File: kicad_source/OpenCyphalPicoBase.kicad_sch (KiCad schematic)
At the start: 49 parts, among them CN1 RASPBERRYPI_PICO, CN11 DNI, CN12 S3B-PH-SM4-TB, CN2 SM04B-SRSS-TB, CN3 SM04B-SRSS-TB, CN6 691322310002, CN7 DNI, CN8 DNI, SW1 PTS636 SM43 SMTR LFS, U3 24LC64-I/SN

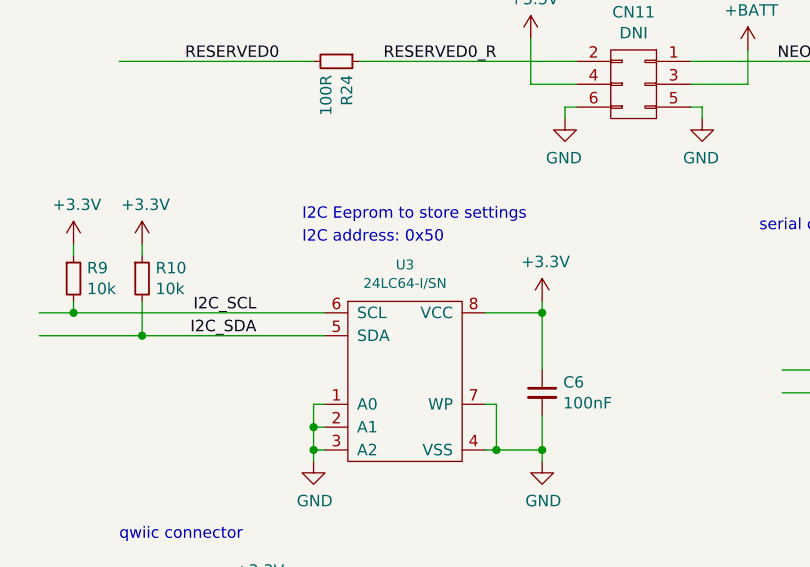
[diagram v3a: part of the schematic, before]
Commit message: switched to JLCPCB basic parts where possible
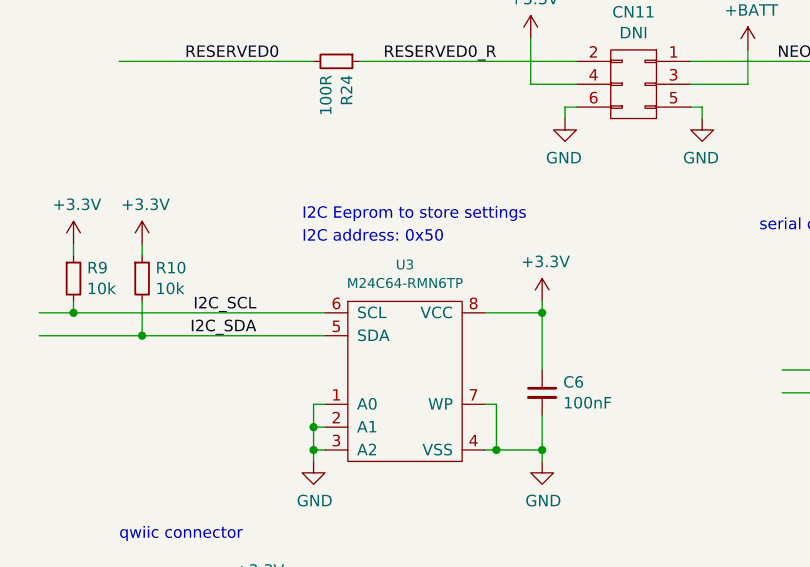
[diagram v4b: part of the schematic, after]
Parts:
- C1, C10, C2, C5, C6, C9: LCSC C314282 -> C14663
- R10, R14, R17, R18, R19, R4, R5, R6, R7, R8, R9: LCSC C3152123 -> C25804
- R11, R12, R20, R21, R22, R23, R24, R25: LCSC C105588 -> C22775
- R15, R16: LCSC C108078 -> C22978
- U3: value 24LC64-I/SN -> M24C64-RMN6TP; LCSC C3007892 -> C79988
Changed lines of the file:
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@@
     )
     (property "Datasheet" "" (id 3) (at 22.86 128.27 0))
-    (property "LCSC" "C3152123" (id 4) (at 22.86 128.27 0)
+    (property "LCSC" "C25804" (id 4) (at 22.86 128.27 0)
       (effects (font (size 1.27 1.27)) hide)
     )
@@
     )
     (property "Datasheet" "" (id 3) (at 30.48 128.27 0))
-    (property "LCSC" "C3152123" (id 4) (at 30.48 128.27 0)
+    (property "LCSC" "C25804" (id 4) (at 30.48 128.27 0)
       (effects (font (size 1.27 1.27)) hide)
     )
@@
     )
     (property "Datasheet" "" (id 3) (at 124.46 166.37 0))
-    (property "LCSC" "C105588" (id 4) (at 124.46 166.37 0)
+    (property "LCSC" "C22775" (id 4) (at 124.46 166.37 0)
       (effects (font (size 1.27 1.27)) hide)
     )
@@
     )
     (property "Datasheet" "" (id 3) (at 85.09 166.37 0))
-    (property "LCSC" "C105588" (id 4) (at 85.09 166.37 0)
+    (property "LCSC" "C22775" (id 4) (at 85.09 166.37 0)
       (effects (font (size 1.27 1.27)) hide)
     )
@@
       (effects (font (size 1.0922 1.0922)))
     )
-    (property "Value" "24LC64-I/SN" (id 1) (at 59.69 128.8034 0)
+    (property "Value" "M24C64-RMN6TP" (id 1) (at 59.69 128.8034 0)
       (effects (font (size 1.0922 1.0922)))
     )
@@
       (effects (font (size 1.0922 1.0922)) hide)
     )
-    (property "LCSC" "C3007892" (id 4) (at 59.69 139.7 0)
+    (property "LCSC" "C79988" (id 4) (at 59.69 139.7 0)
       (effects (font (size 1.27 1.27)) hide)
     )
@@
     )
     (property "Datasheet" "" (id 3) (at 74.93 140.97 0))
-    (property "LCSC" "C314282" (id 4) (at 74.93 140.97 0)
+    (property "LCSC" "C14663" (id 4) (at 74.93 140.97 0)
       (effects (font (size 1.27 1.27)) hide)
     )
@@
     )
     (property "Datasheet" "" (id 3) (at 259.08 63.5 0))
-    (property "LCSC" "C108078" (id 4) (at 259.08 63.5 0)
+    (property "LCSC" "C22978" (id 4) (at 259.08 63.5 0)
       (effects (font (size 1.27 1.27)) hide)
     )
@@
     )
     (property "Datasheet" "" (id 3) (at 270.51 63.5 0))
-    (property "LCSC" "C108078" (id 4) (at 270.51 63.5 0)
+    (property "LCSC" "C22978" (id 4) (at 270.51 63.5 0)
       (effects (font (size 1.27 1.27)) hide)
     )
@@
     )
     (property "Datasheet" "" (id 3) (at 256.54 38.1 0))
-    (property "LCSC" "C3152123" (id 4) (at 256.54 38.1 0)
+    (property "LCSC" "C25804" (id 4) (at 256.54 38.1 0)
       (effects (font (size 1.27 1.27)) hide)
     )
@@
     )
     (property "Datasheet" "" (id 3) (at 265.43 38.1 0))
-    (property "LCSC" "C314282" (id 4) (at 265.43 38.1 0)
+    (property "LCSC" "C14663" (id 4) (at 265.43 38.1 0)
       (effects (font (size 1.27 1.27)) hide)
     )
@@
     )
     (property "Datasheet" "" (id 3) (at 48.26 20.32 0))
-    (property "LCSC" "C3152123" (id 4) (at 48.26 20.32 0)
+    (property "LCSC" "C25804" (id 4) (at 48.26 20.32 0)
       (effects (font (size 1.27 1.27)) hide)
     )
@@
     )
     (property "Datasheet" "" (id 3) (at 55.88 20.32 0))
-    (property "LCSC" "C3152123" (id 4) (at 55.88 20.32 0)
+    (property "LCSC" "C25804" (id 4) (at 55.88 20.32 0)
       (effects (font (size 1.27 1.27)) hide)
     )
@@
     )
     (property "Datasheet" "" (id 3) (at 63.5 20.32 0))
-    (property "LCSC" "C3152123" (id 4) (at 63.5 20.32 0)
+    (property "LCSC" "C25804" (id 4) (at 63.5 20.32 0)
       (effects (font (size 1.27 1.27)) hide)
     )
@@
     )
     (property "Datasheet" "" (id 3) (at 71.12 20.32 0))
-    (property "LCSC" "C3152123" (id 4) (at 71.12 20.32 0)
+    (property "LCSC" "C25804" (id 4) (at 71.12 20.32 0)
       (effects (font (size 1.27 1.27)) hide)
     )
@@
     )
     (property "Datasheet" "" (id 3) (at 76.2 24.13 0))
-    (property "LCSC" "C3152123" (id 4) (at 76.2 24.13 0)
+    (property "LCSC" "C25804" (id 4) (at 76.2 24.13 0)
       (effects (font (size 1.27 1.27)) hide)
     )
@@
     )
     (property "Datasheet" "" (id 3) (at 76.2 29.21 0))
-    (property "LCSC" "C3152123" (id 4) (at 76.2 29.21 0)
+    (property "LCSC" "C25804" (id 4) (at 76.2 29.21 0)
       (effects (font (size 1.27 1.27)) hide)
     )
@@
     )
     (property "Datasheet" "" (id 3) (at 76.2 34.29 0))
-    (property "LCSC" "C3152123" (id 4) (at 76.2 34.29 0)
+    (property "LCSC" "C25804" (id 4) (at 76.2 34.29 0)
       (effects (font (size 1.27 1.27)) hide)
     )
@@
     )
     (property "Datasheet" "" (id 3) (at 76.2 39.37 0))
-    (property "LCSC" "C3152123" (id 4) (at 76.2 39.37 0)
+    (property "LCSC" "C25804" (id 4) (at 76.2 39.37 0)
       (effects (font (size 1.27 1.27)) hide)
     )
@@
     )
     (property "Datasheet" "" (id 3) (at 86.36 44.45 0))
-    (property "LCSC" "C314282" (id 4) (at 86.36 44.45 0)
+    (property "LCSC" "C14663" (id 4) (at 86.36 44.45 0)
       (effects (font (size 1.27 1.27)) hide)
     )
@@
     )
     (property "Datasheet" "" (id 3) (at 96.52 44.45 0))
-    (property "LCSC" "C314282" (id 4) (at 96.52 44.45 0)
+    (property "LCSC" "C14663" (id 4) (at 96.52 44.45 0)
       (effects (font (size 1.27 1.27)) hide)
     )
@@
     )
     (property "Datasheet" "" (id 3) (at 106.68 44.45 0))
-    (property "LCSC" "C314282" (id 4) (at 106.68 44.45 0)
+    (property "LCSC" "C14663" (id 4) (at 106.68 44.45 0)
       (effects (font (size 1.27 1.27)) hide)
     )
@@
     )
     (property "Datasheet" "" (id 3) (at 116.84 44.45 0))
-    (property "LCSC" "C314282" (id 4) (at 116.84 44.45 0)
+    (property "LCSC" "C14663" (id 4) (at 116.84 44.45 0)
       (effects (font (size 1.27 1.27)) hide)
     )
@@
     )
     (property "Datasheet" "" (id 3) (at 60.96 60.96 0))
-    (property "LCSC" "C105588" (id 4) (at 60.96 60.96 0)
+    (property "LCSC" "C22775" (id 4) (at 60.96 60.96 0)
       (effects (font (size 1.27 1.27)) hide)
     )
@@
     )
     (property "Datasheet" "" (id 3) (at 60.96 66.04 0))
-    (property "LCSC" "C105588" (id 4) (at 60.96 66.04 0)
+    (property "LCSC" "C22775" (id 4) (at 60.96 66.04 0)
       (effects (font (size 1.27 1.27)) hide)
     )
@@
     )
     (property "Datasheet" "" (id 3) (at 74.93 78.74 0))
-    (property "LCSC" "C105588" (id 4) (at 74.93 78.74 0)
+    (property "LCSC" "C22775" (id 4) (at 74.93 78.74 0)
       (effects (font (size 1.27 1.27)) hide)
     )
@@
     )
     (property "Datasheet" "" (id 3) (at 74.93 83.82 0))
-    (property "LCSC" "C105588" (id 4) (at 74.93 83.82 0)
+    (property "LCSC" "C22775" (id 4) (at 74.93 83.82 0)
       (effects (font (size 1.27 1.27)) hide)
     )
@@
     )
     (property "Datasheet" "" (id 3) (at 52.07 104.14 0))
-    (property "LCSC" "C105588" (id 4) (at 52.07 104.14 0)
+    (property "LCSC" "C22775" (id 4) (at 52.07 104.14 0)
       (effects (font (size 1.27 1.27)) hide)
     )
@@
     )
     (property "Datasheet" "" (id 3) (at 115.57 104.14 0))
-    (property "LCSC" "C105588" (id 4) (at 115.57 104.14 0)
+    (property "LCSC" "C22775" (id 4) (at 115.57 104.14 0)
       (effects (font (size 1.27 1.27)) hide)
     )
@@
     )
     (path "/00000000-0000-0000-0000-00006251b961"
-      (reference "U3") (unit 1) (value "24LC64-I/SN") (footprint "Package_SO:SOIC-8_3.9x4.9mm_P1.27mm")
+      (reference "U3") (unit 1) (value "M24C64-RMN6TP") (footprint "Package_SO:SOIC-8_3.9x4.9mm_P1.27mm")
     )
     (path "/00000000-0000-0000-0000-00005ed92f9c/00000000-0000-0000-0000-00005ed9419d"
@@
     )
     (path "/00000000-0000-0000-0000-00005ed92f9c/00000000-0000-0000-0000-00005edabfb3"
-      (reference "U9") (unit 1) (value "SN65HVD232") (footprint "Package_SO:SOIC-8_3.9x4.9mm_P1.27mm")
+      (reference "U9") (unit 1) (value "SN65HVD230") (footprint "Package_SO:SOIC-8_3.9x4.9mm_P1.27mm")
     )
     (path "/00000000-0000-0000-0000-00005ed92f9c/00000000-0000-0000-0000-00005ed95d76"
